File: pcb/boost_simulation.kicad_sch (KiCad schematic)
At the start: 10 parts, among them Q1 2N5104, Q2 NMOS

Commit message: More notes
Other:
- note added: "50Khz 97.5% PWM best guess"
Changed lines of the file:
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@@
     (stroke (width 0) (type default))
+  )
+  (text "50Khz 97.5% PWM\nbest guess" (at 101.6 116.84 0)
+    (effects (font (size 1.27 1.27)) (justify left bottom))
   )
   (text "typical internal\nAA resistance" (at 77.47 69.85 0)

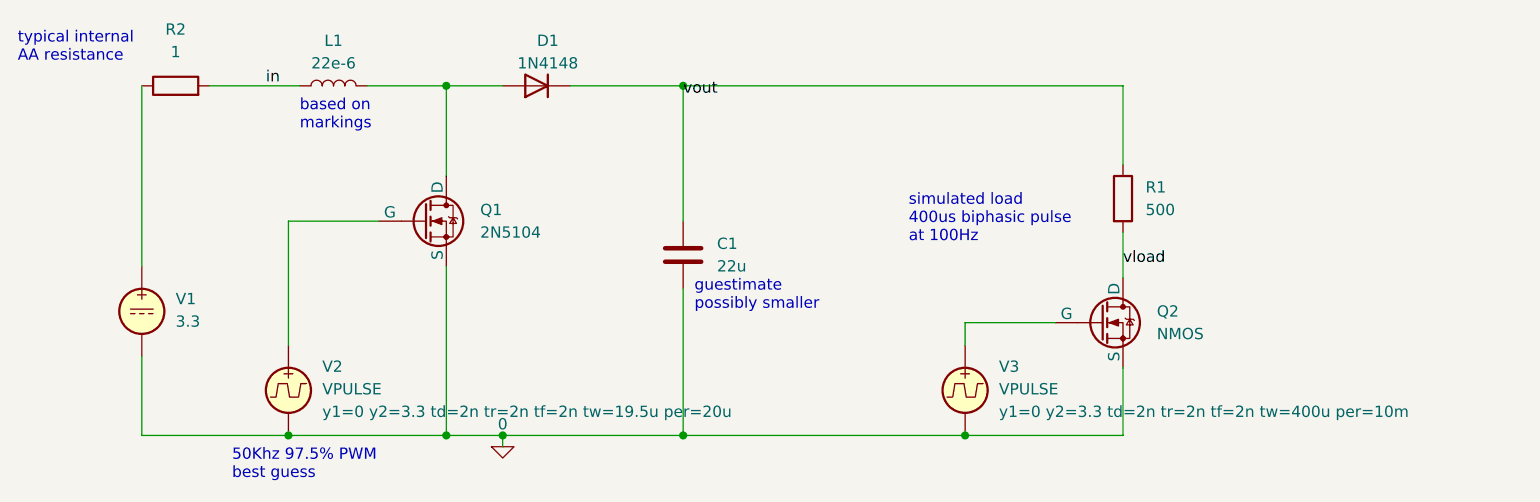
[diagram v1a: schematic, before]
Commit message: Updated sim results from teardown
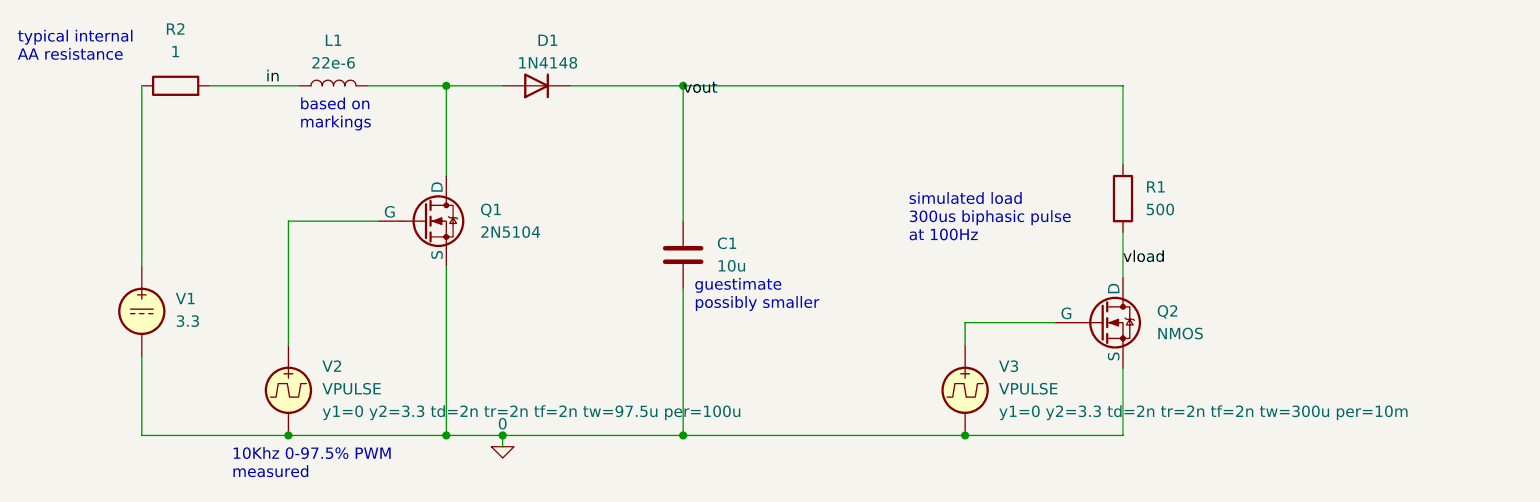
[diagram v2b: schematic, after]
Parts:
- C1: value 22u -> 10u
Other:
- note added: "10Khz 0-97.5% PWM measured"
- note added: "simulated load 300us biphasic pulse at 100Hz"
- note removed: "50Khz 97.5% PWM best guess"
- note removed: "simulated load 400us biphasic pulse at 100Hz"
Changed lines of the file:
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@@
     (stroke (width 0) (type default))
   )
-  (text "50Khz 97.5% PWM\nbest guess" (at 101.6 116.84 0)
+  (text "10Khz 0-97.5% PWM\nmeasured" (at 101.6 116.84 0)
     (effects (font (size 1.27 1.27)) (justify left bottom))
   )
@@
     (effects (font (size 1.27 1.27)) (justify left bottom))
   )
-  (text "simulated load\n400us biphasic pulse\nat 100Hz" (at 177.8 90.17 0)
+  (text "simulated load\n300us biphasic pulse\nat 100Hz" (at 177.8 90.17 0)
     (effects (font (size 1.27 1.27)) (justify left bottom))
   )
@@
       (effects (font (size 1.27 1.27)) (justify left) hide)
     )
-    (property "Sim.Params" "y1=0 y2=3.3 td=2n tr=2n tf=2n tw=19.5u per=20u" (at 111.76 109.0902 0)
+    (property "Sim.Params" "y1=0 y2=3.3 td=2n tr=2n tf=2n tw=97.5u per=100u" (at 111.76 109.0902 0)
       (effects (font (size 1.27 1.27)) (justify left))
     )
@@
       (effects (font (size 1.27 1.27)) (justify left) hide)
     )
-    (property "Sim.Params" "y1=0 y2=3.3 td=2n tr=2n tf=2n tw=400u per=10m" (at 187.96 109.0902 0)
+    (property "Sim.Params" "y1=0 y2=3.3 td=2n tr=2n tf=2n tw=300u per=10m" (at 187.96 109.0902 0)
       (effects (font (size 1.27 1.27)) (justify left))
     )
@@
       (effects (font (size 1.27 1.27)) (justify left))
     )
-    (property "Value" "22u" (at 156.21 92.71 0)
-      (effects (font (size 1.27 1.27)) (justify left))
-    )
+    (property "Value" "10u" (at 156.21 92.71 0)
+      (effects (font (size 1.27 1.27)) (justify left))
+    )
